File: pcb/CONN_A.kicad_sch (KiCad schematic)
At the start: 1 part, among them J1 6437288-4

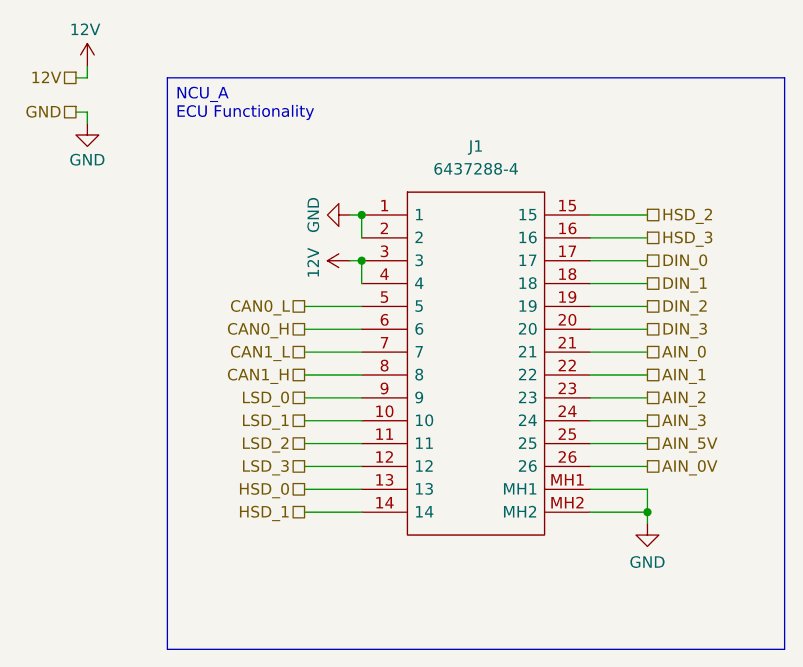
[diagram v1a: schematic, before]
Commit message: removed AGND and added ground garden
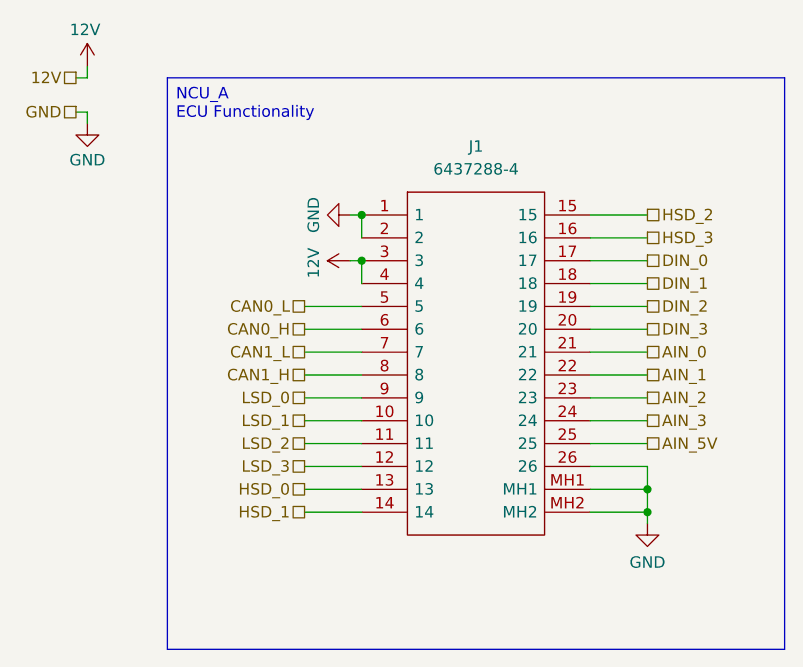
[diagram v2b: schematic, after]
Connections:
- net AIN_0V is gone; now on net GND: J1.26
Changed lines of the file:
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@@
+	)
+	(junction
+		(at 90.17 71.12)
+		(diameter 0)
+		(color 0 0 0 0)
 	)
 	(junction
@@
 	(wire
 		(pts
+			(xy 83.82 48.26) (xy 90.17 48.26)
+		)
+		(stroke
+			(width 0)
+			(type default)
+		)
+	)
+	(wire
+		(pts
+			(xy 83.82 66.04) (xy 90.17 66.04)
+		)
+		(stroke
+			(width 0)
+			(type default)
+		)
+	)
+	(wire
+		(pts
+			(xy 83.82 55.88) (xy 90.17 55.88)
+		)
+		(stroke
+			(width 0)
+			(type default)
+		)
+	)
+	(wire
+		(pts
+			(xy 52.07 66.04) (xy 58.42 66.04)
+		)
+		(stroke
+			(width 0)
+			(type default)
+		)
+	)
+	(wire
+		(pts
+			(xy 90.17 73.66) (xy 90.17 74.93)
+		)
+		(stroke
+			(width 0)
+			(type default)
+		)
+	)
+	(wire
+		(pts
+			(xy 52.07 58.42) (xy 58.42 58.42)
+		)
+		(stroke
+			(width 0)
+			(type default)
+		)
+	)
+	(wire
+		(pts
+			(xy 83.82 50.8) (xy 90.17 50.8)
+		)
+		(stroke
+			(width 0)
+			(type default)
+		)
+	)
+	(wire
+		(pts
+			(xy 83.82 73.66) (xy 90.17 73.66)
+		)
+		(stroke
+			(width 0)
+			(type default)
+		)
+	)
+	(wire
+		(pts
+			(xy 83.82 43.18) (xy 90.17 43.18)
+		)
+		(stroke
+			(width 0)
+			(type default)
+		)
+	)
+	(wire
+		(pts
+			(xy 58.42 43.18) (xy 58.42 40.64)
+		)
+		(stroke
+			(width 0)
+			(type default)
+		)
+	)
+	(wire
+		(pts
+			(xy 83.82 58.42) (xy 90.17 58.42)
+		)
+		(stroke
+			(width 0)
+			(type default)
+		)
+	)
+	(wire
+		(pts
+			(xy 57.15 40.64) (xy 58.42 40.64)
+		)
+		(stroke
+			(width 0)
+			(type default)
+		)
+	)
+	(wire
+		(pts
+			(xy 52.07 50.8) (xy 58.42 50.8)
+		)
+		(stroke
+			(width 0)
+			(type default)
+		)
+	)
+	(wire
+		(pts
+			(xy 52.07 63.5) (xy 58.42 63.5)
+		)
+		(stroke
+			(width 0)
+			(type default)
+		)
+	)
+	(wire
+		(pts
+			(xy 27.94 30.48) (xy 27.94 29.21)
+		)
+		(stroke
+			(width 0)
+			(type default)
+		)
+	)
+	(wire
+		(pts
+			(xy 83.82 40.64) (xy 90.17 40.64)
+		)
+		(stroke
+			(width 0)
+			(type default)
+		)
+	)
+	(wire
+		(pts
+			(xy 83.82 71.12) (xy 90.17 71.12)
+		)
+		(stroke
+			(width 0)
+			(type default)
+		)
+	)
+	(wire
+		(pts
+			(xy 90.17 71.12) (xy 90.17 73.66)
+		)
+		(stroke
+			(width 0)
+			(type default)
+		)
+	)
+	(wire
+		(pts
 			(xy 83.82 68.58) (xy 90.17 68.58)
 		)
@@
 	(wire
 		(pts
-			(xy 83.82 48.26) (xy 90.17 48.26)
-		)
-		(stroke
-			(width 0)
-			(type default)
-		)
-	)
-	(wire
-		(pts
-			(xy 83.82 66.04) (xy 90.17 66.04)
-		)
-		(stroke
-			(width 0)
-			(type default)
-		)
-	)
-	(wire
-		(pts
-			(xy 83.82 55.88) (xy 90.17 55.88)
-		)
-		(stroke
-			(width 0)
-			(type default)
-		)
-	)
-	(wire
-		(pts
-			(xy 52.07 66.04) (xy 58.42 66.04)
-		)
-		(stroke
-			(width 0)
-			(type default)
-		)
-	)
-	(wire
-		(pts
-			(xy 90.17 73.66) (xy 90.17 74.93)
-		)
-		(stroke
-			(width 0)
-			(type default)
-		)
-	)
-	(wire
-		(pts
-			(xy 52.07 58.42) (xy 58.42 58.42)
-		)
-		(stroke
-			(width 0)
-			(type default)
-		)
-	)
-	(wire
-		(pts
-			(xy 83.82 50.8) (xy 90.17 50.8)
-		)
-		(stroke
-			(width 0)
-			(type default)
-		)
-	)
-	(wire
-		(pts
-			(xy 83.82 73.66) (xy 90.17 73.66)
-		)
-		(stroke
-			(width 0)
-			(type default)
-		)
-	)
-	(wire
-		(pts
-			(xy 83.82 43.18) (xy 90.17 43.18)
-		)
-		(stroke
-			(width 0)
-			(type default)
-		)
-	)
-	(wire
-		(pts
-			(xy 58.42 43.18) (xy 58.42 40.64)
-		)
-		(stroke
-			(width 0)
-			(type default)
-		)
-	)
-	(wire
-		(pts
-			(xy 83.82 58.42) (xy 90.17 58.42)
-		)
-		(stroke
-			(width 0)
-			(type default)
-		)
-	)
-	(wire
-		(pts
-			(xy 57.15 40.64) (xy 58.42 40.64)
-		)
-		(stroke
-			(width 0)
-			(type default)
-		)
-	)
-	(wire
-		(pts
-			(xy 52.07 50.8) (xy 58.42 50.8)
-		)
-		(stroke
-			(width 0)
-			(type default)
-		)
-	)
-	(wire
-		(pts
-			(xy 52.07 63.5) (xy 58.42 63.5)
-		)
-		(stroke
-			(width 0)
-			(type default)
-		)
-	)
-	(wire
-		(pts
-			(xy 27.94 30.48) (xy 27.94 29.21)
-		)
-		(stroke
-			(width 0)
-			(type default)
-		)
-	)
-	(wire
-		(pts
-			(xy 83.82 40.64) (xy 90.17 40.64)
-		)
-		(stroke
-			(width 0)
-			(type default)
-		)
-	)
-	(wire
-		(pts
-			(xy 83.82 71.12) (xy 90.17 71.12)
-		)
-		(stroke
-			(width 0)
-			(type default)
-		)
-	)
-	(wire
-		(pts
-			(xy 90.17 71.12) (xy 90.17 73.66)
-		)
-		(stroke
-			(width 0)
-			(type default)
-		)
-	)
-	(wire
-		(pts
 			(xy 83.82 63.5) (xy 90.17 63.5)
 		)
@@
 		(pts
 			(xy 52.07 68.58) (xy 58.42 68.58)
+		)
+		(stroke
+			(width 0)
+			(type default)
+		)
+	)
+	(wire
+		(pts
+			(xy 90.17 68.58) (xy 90.17 71.12)
 		)
 		(stroke
@@
 		(effects
 			(font
-				(size 1.27 1.27)
-			)
-			(justify left)
-		)
-	)
-	(hierarchical_label "AIN_0V"
-		(shape passive)
-		(at 90.17 68.58 0)
-		(effects
-			(font

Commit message: changed conn a pinout
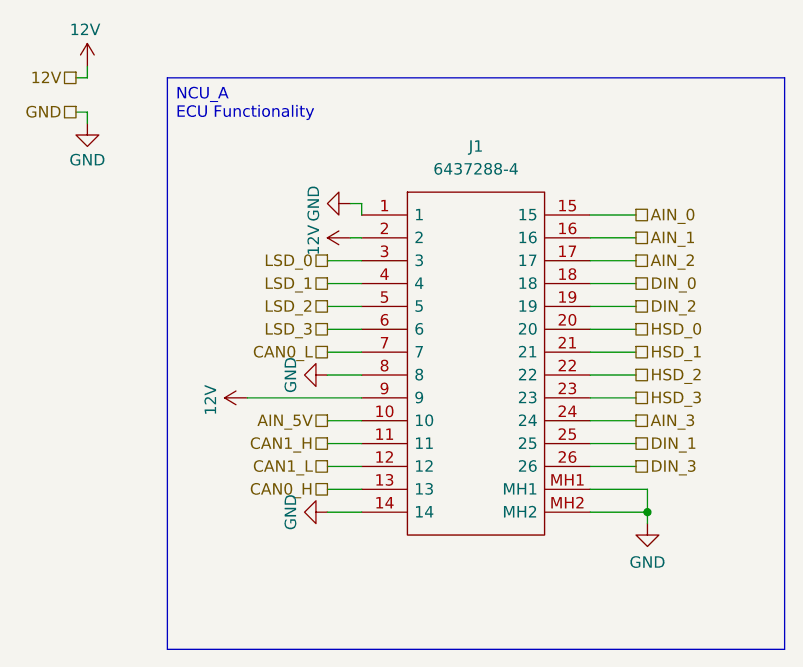
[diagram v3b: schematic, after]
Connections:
- net 12V: now also J1.2, J1.9; no longer J1.3, J1.4
- net AIN_0: now also J1.15; no longer J1.21
- net AIN_1: now also J1.16; no longer J1.22
- net AIN_2: now also J1.17; no longer J1.23
- net AIN_5V: now also J1.10; no longer J1.25
- net CAN0_H: now also J1.13; no longer J1.6
- net CAN0_L: now also J1.7; no longer J1.5
- net CAN1_H: now also J1.11; no longer J1.8
- net CAN1_L: now also J1.12; no longer J1.7
- net DIN_0: now also J1.18; no longer J1.17
- net DIN_1: now also J1.25; no longer J1.18
- net DIN_3: now also J1.26; no longer J1.20
- net GND: now also J1.14, J1.8; no longer J1.2, J1.26
- net HSD_0: now also J1.20; no longer J1.13
- net HSD_1: now also J1.21; no longer J1.14
- net HSD_2: now also J1.22; no longer J1.15
- net HSD_3: now also J1.23; no longer J1.16
- net LSD_0: now also J1.3; no longer J1.9
- net LSD_1: now also J1.4; no longer J1.10
- net LSD_2: now also J1.5; no longer J1.11
- net LSD_3: now also J1.6; no longer J1.12
